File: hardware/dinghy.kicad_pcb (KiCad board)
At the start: 2 copper layers, 105.5 x 88.9 mm, 56 parts, among them J10 Header 1, J11 Header 2, J2 Fan 1, J3 Fan2, J4 Motor, J5 Endtemp, J6 Endstop, J7 PGM, J8 UART, J9 Power, Q1 IRLR7843PbF, Q2 IRLR7843PbF, Q3 IRLR7843PbF, SW1 SW_Push, U1 TMC2130, U2 ATMEGA1284P-AU, Y1 Crystal

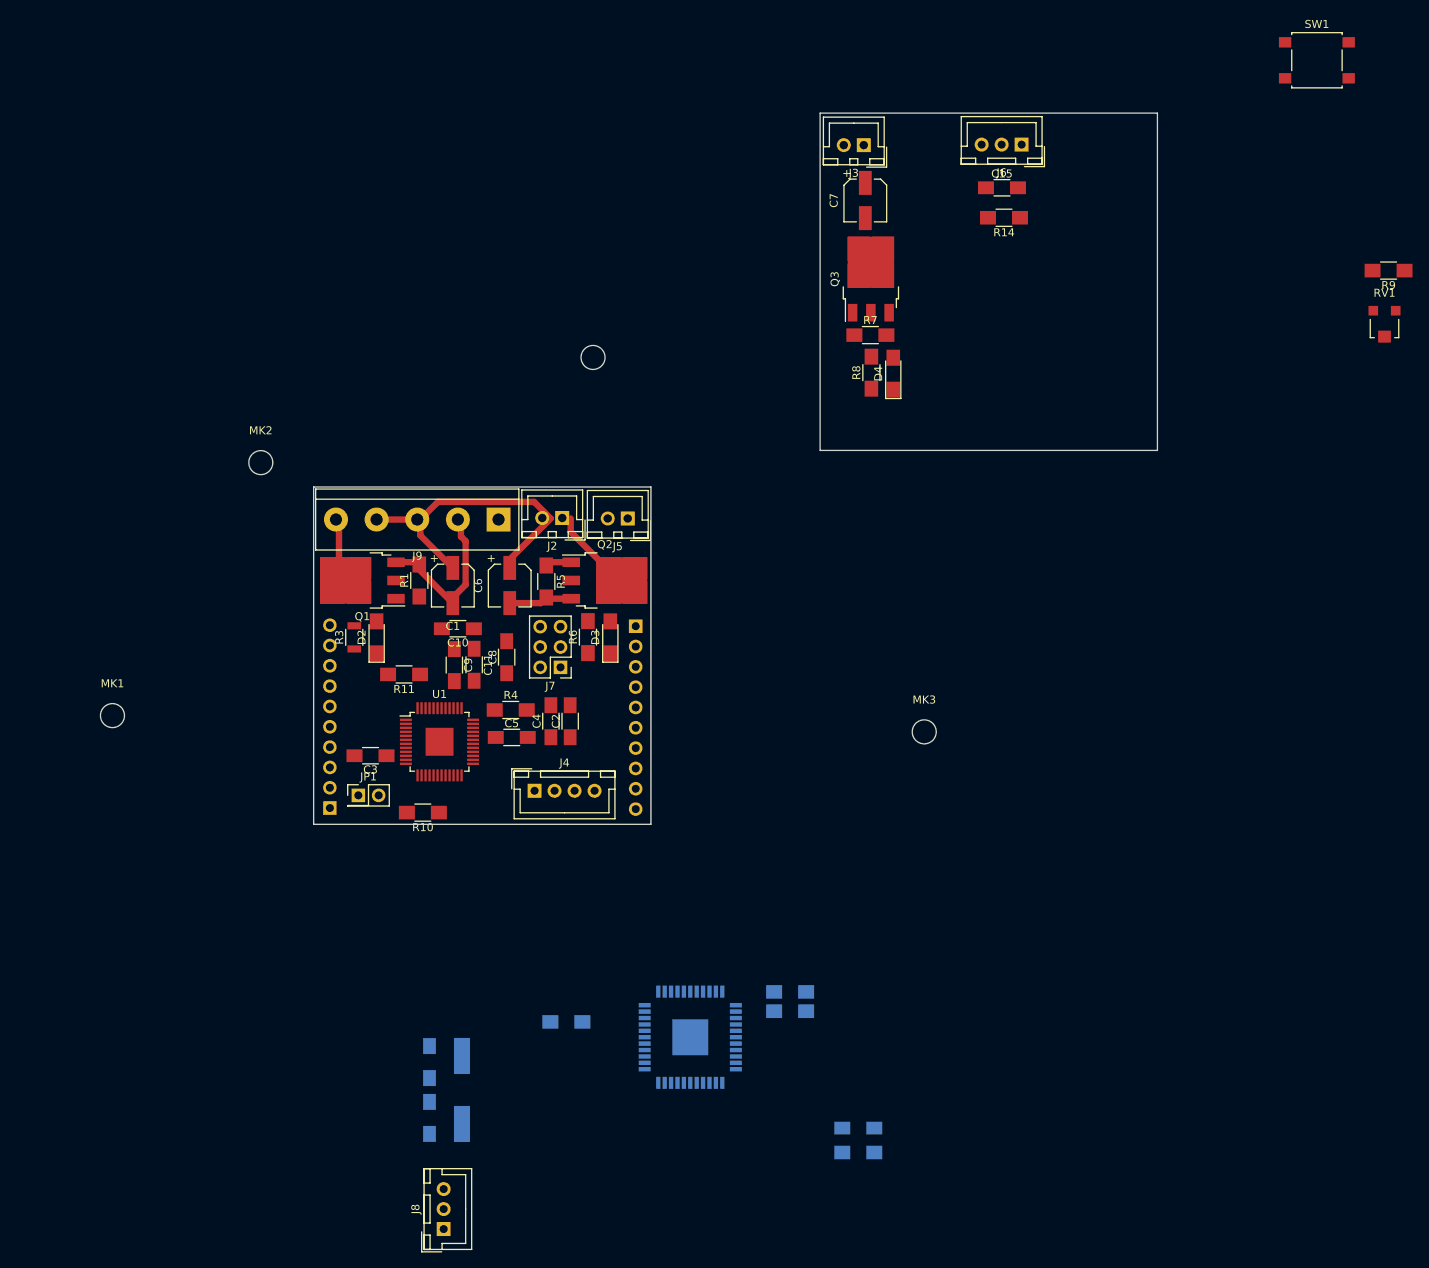
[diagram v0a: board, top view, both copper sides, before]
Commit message: Renamed power net
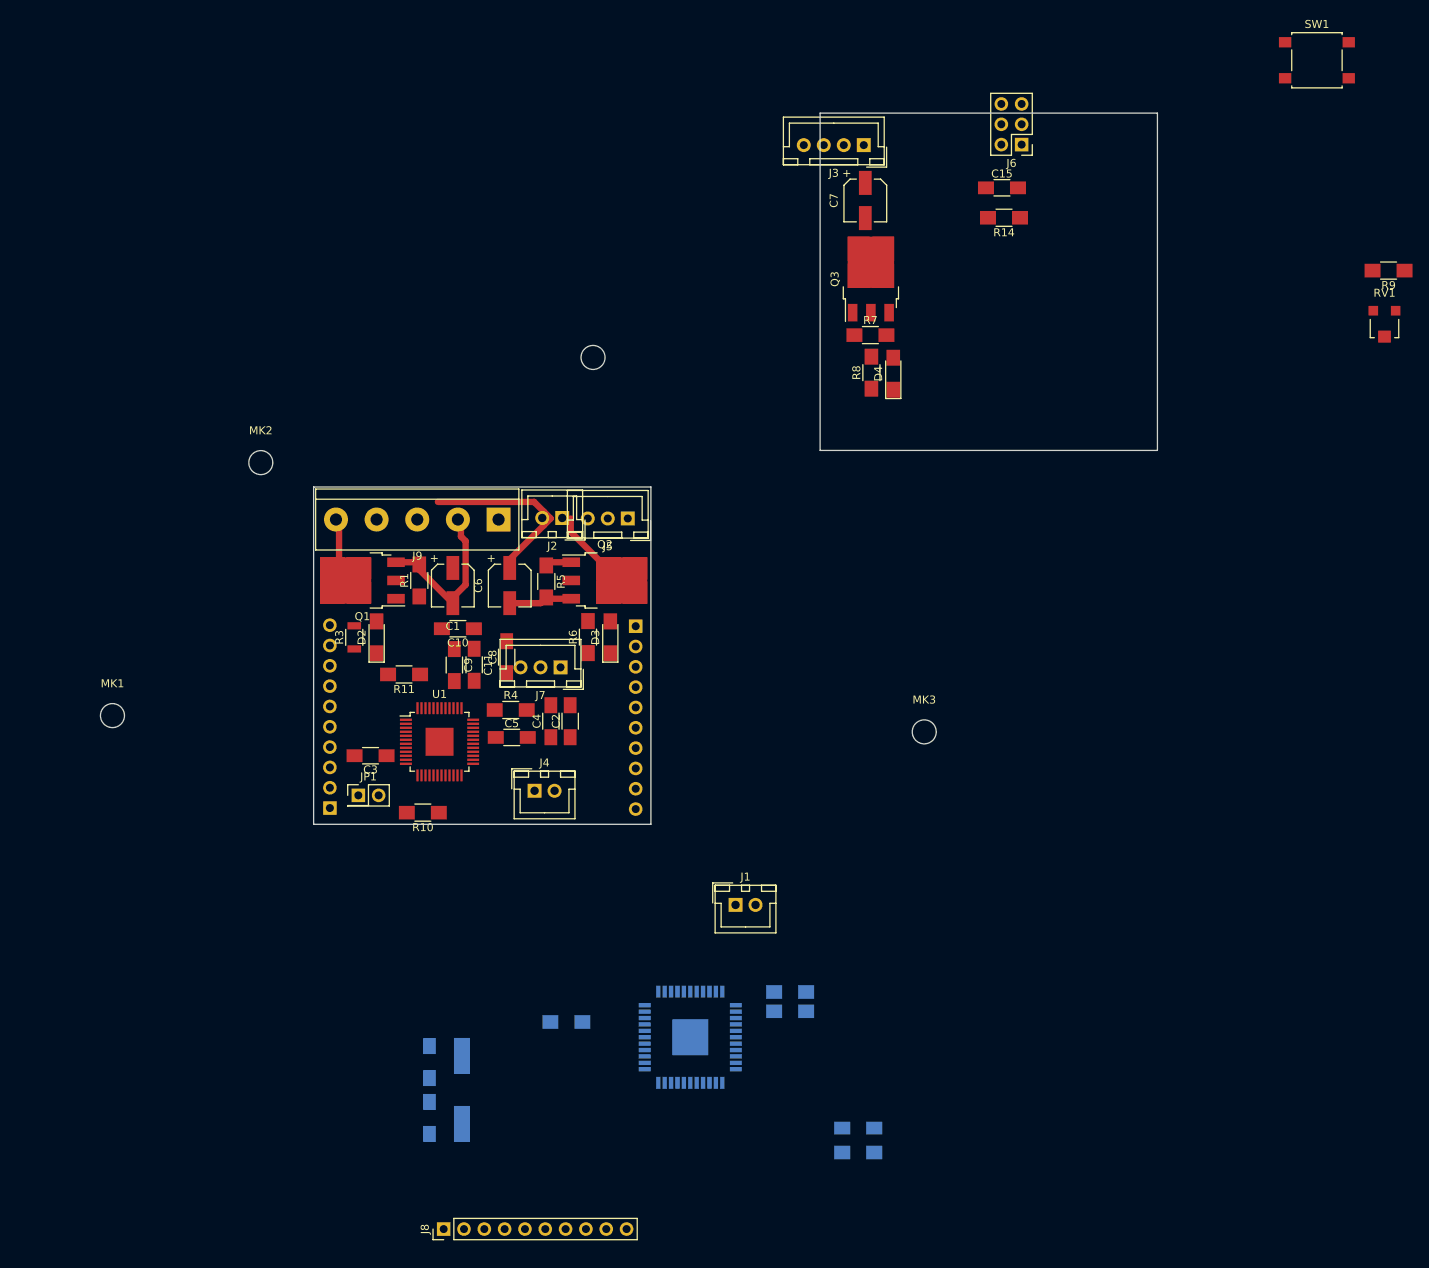
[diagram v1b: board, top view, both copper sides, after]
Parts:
- added J1: Fan 1, Connectors_JST:JST_XH_B02B-XH-A_02x2.50mm_Straight, F.Cu at (177.2, 131.5)
- C10: value 1µ/50V -> 100n/50V
- C11: value 100n/50V -> 1µ/50V
- J10: value Header 1 -> Header 2
- J2: value Fan 1 -> Fan2
- J3: value Fan2 -> Motor; footprint Connectors_JST:JST_XH_B02B-XH-A_02x2.50mm_Straight -> Connectors_JST:JST_XH_B04B-XH-A_04x2.50mm_Straight
- J4: value Motor -> Endtemp; footprint Connectors_JST:JST_XH_B04B-XH-A_04x2.50mm_Straight -> Connectors_JST:JST_XH_B02B-XH-A_02x2.50mm_Straight
- J5: value Endtemp -> Endstop; footprint Connectors_JST:JST_XH_B02B-XH-A_02x2.50mm_Straight -> Connectors_JST:JST_XH_B03B-XH-A_03x2.50mm_Straight
- J6: value Endstop -> PGM; footprint Connectors_JST:JST_XH_B03B-XH-A_03x2.50mm_Straight -> Pin_Headers:Pin_Header_Straight_2x03_Pitch2.54mm
- J7: value PGM -> UART; footprint Pin_Headers:Pin_Header_Straight_2x03_Pitch2.54mm -> Connectors_JST:JST_XH_B03B-XH-A_03x2.50mm_Straight
- J8: value UART -> Header 1; footprint Connectors_JST:JST_XH_B03B-XH-A_03x2.50mm_Straight -> Pin_Headers:Pin_Header_Straight_1x10_Pitch2.54mm
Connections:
- C1 pad 1: +12V -> VMot
- C10 pad 1: GND -> VMot
- C10 pad 2: +12V -> Net-(C10-Pad2)
- C11 pad 1: +12V -> GND
- C11 pad 2: Net-(C11-Pad2) -> VMot
- C2 pad 2: +12V -> VMot
- C6 pad 1: +12V -> VMot
- C7 pad 1: +12V -> VMot
- C9 pad 2: +12V -> VMot
- D2 pad 2: +12V -> VMot
- D3 pad 2: +12V -> VMot
- D4 pad 2: +12V -> VMot
- J10 pad 1: /PA4 -> VMot
- J10 pad 10: /SCL -> /PD4
- J10 pad 2: /PA3 -> VMot
- J10 pad 3: /PA2 -> GND
- J10 pad 4: /PA1 -> GND
- J10 pad 5: /PA0 -> +5V
- J10 pad 6: /TXD1 -> /FAN2
- J10 pad 7: /RXD1 -> /ENDSTOP
- J10 pad 8: GND -> /PD7
- J10 pad 9: /SDA -> /PD6
- J11 pad 1: /12V -> +12V
- J11 pad 2: /12V -> +12V
- J11 pad 5: (no net) -> +5V
- J2 pad 2: +12V -> VMot
- J3 pad 1: Net-(J3-Pad1) -> /OB2
- J3 pad 2: +12V -> /OB1
- J4 pad 1: /OB2 -> GND
- J4 pad 2: /OB1 -> /ENDTEMP
- J5 pad 2: /ENDTEMP -> +5V
- J6 pad 1: GND -> /MISO
- J6 pad 3: /ENDSTOP -> /SCK
- J7 pad 1: /MISO -> /TXD0
- J7 pad 2: +5V -> GND
- J7 pad 3: /SCK -> /RXD0
- J8 pad 1: /TXD0 -> /PA4
- J8 pad 2: GND -> /PA3
- J8 pad 3: /RXD0 -> /PA2
- J9 pad 3: +12V -> VMot
- J9 pad 4: +12V -> VMot
- Q2 pad 2: Net-(J2-Pad1) -> Net-(J1-Pad1)
- Q3 pad 2: Net-(J3-Pad1) -> Net-(J2-Pad1)
- R6 pad 2: Net-(J2-Pad1) -> Net-(J1-Pad1)
- R8 pad 2: Net-(J3-Pad1) -> Net-(J2-Pad1)
- U1 pad 21: +12V -> VMot
- U1 pad 24: (no net) -> /M-DCEN
- U1 pad 27: (no net) -> /M-DIAG1
- U1 pad 38: Net-(C11-Pad2) -> Net-(C10-Pad2)
- U1 pad 39: +12V -> VMot
- U1 pad 40: +12V -> VMot
- U2 pad 22: (no net) -> /M-DCEN
- U2 pad 26: (no net) -> /M-DIAG1
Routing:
- net +12V: track 39.2 -> 0.00 mm
- net VMot: track 0.00 -> 23.3 mm
- net Net-(J2-Pad1): track 8.26 -> 0.00 mm
- net Net-(J1-Pad1): track 0.00 -> 8.26 mm

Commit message: Basic layout done.
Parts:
- removed J11: Header 2, Pin_Headers:Pin_Header_Straight_1x10_Pitch2.54mm
- D1, MK4, R2: moved to F.Cu
- J8: moved to B.Cu
- R3: footprint Resistors_SMD:R_1206 -> Resistors_SMD:R_1206_HandSoldering
- moved J6 111.2 mm to (135.5, 116.2), turned to 270 degrees
- moved J3 96.1 mm to (141.5, 117.5), turned to 0 degrees
- moved C12 65.9 mm to (147.0, 92.7), turned to 180 degrees
- moved C13 60.4 mm to (154.0, 92.7), turned to 0 degrees
- moved J5 60.2 mm to (216.1, 53.6)
- moved Y1 58.4 mm to (150.5, 96.7), turned to 180 degrees
- moved J8 54.8 mm to (126.4, 119.1), turned to 0 degrees
- moved J1 54.3 mm to (153.0, 82.9)
- moved D1 46.9 mm to (158.7, 105.3), turned to 270 degrees
- moved U2 44.7 mm to (155.0, 106.5), turned to 270 degrees
- moved R2 43.4 mm to (161.5, 105.3), turned to 270 degrees
- moved JP1 41.5 mm to (88.6, 115.3), turned to 270 degrees
- moved R12 41.1 mm to (175.4, 109.8), turned to 180 degrees
- moved J2 37.6 mm to (183.2, 57.7)
- moved J4 35.5 mm to (161.2, 82.9)
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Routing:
- net GND: track 29.0 -> 0.00 mm
- net VMot: track 23.3 -> 0.00 mm
- net Net-(J1-Pad1): track 8.26 -> 0.00 mm
- net /HOTEND-: track 6.45 -> 0.00 mm
- net /FAN1: track 3.29 -> 0.00 mm
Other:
- net class Digital added: clearance 0.2, trace_width 0.2, via_dia 0.6, via_drill 0.4
- net class Power added: clearance 0.3, trace_width 0.8, via_dia 0.6, via_drill 0.4

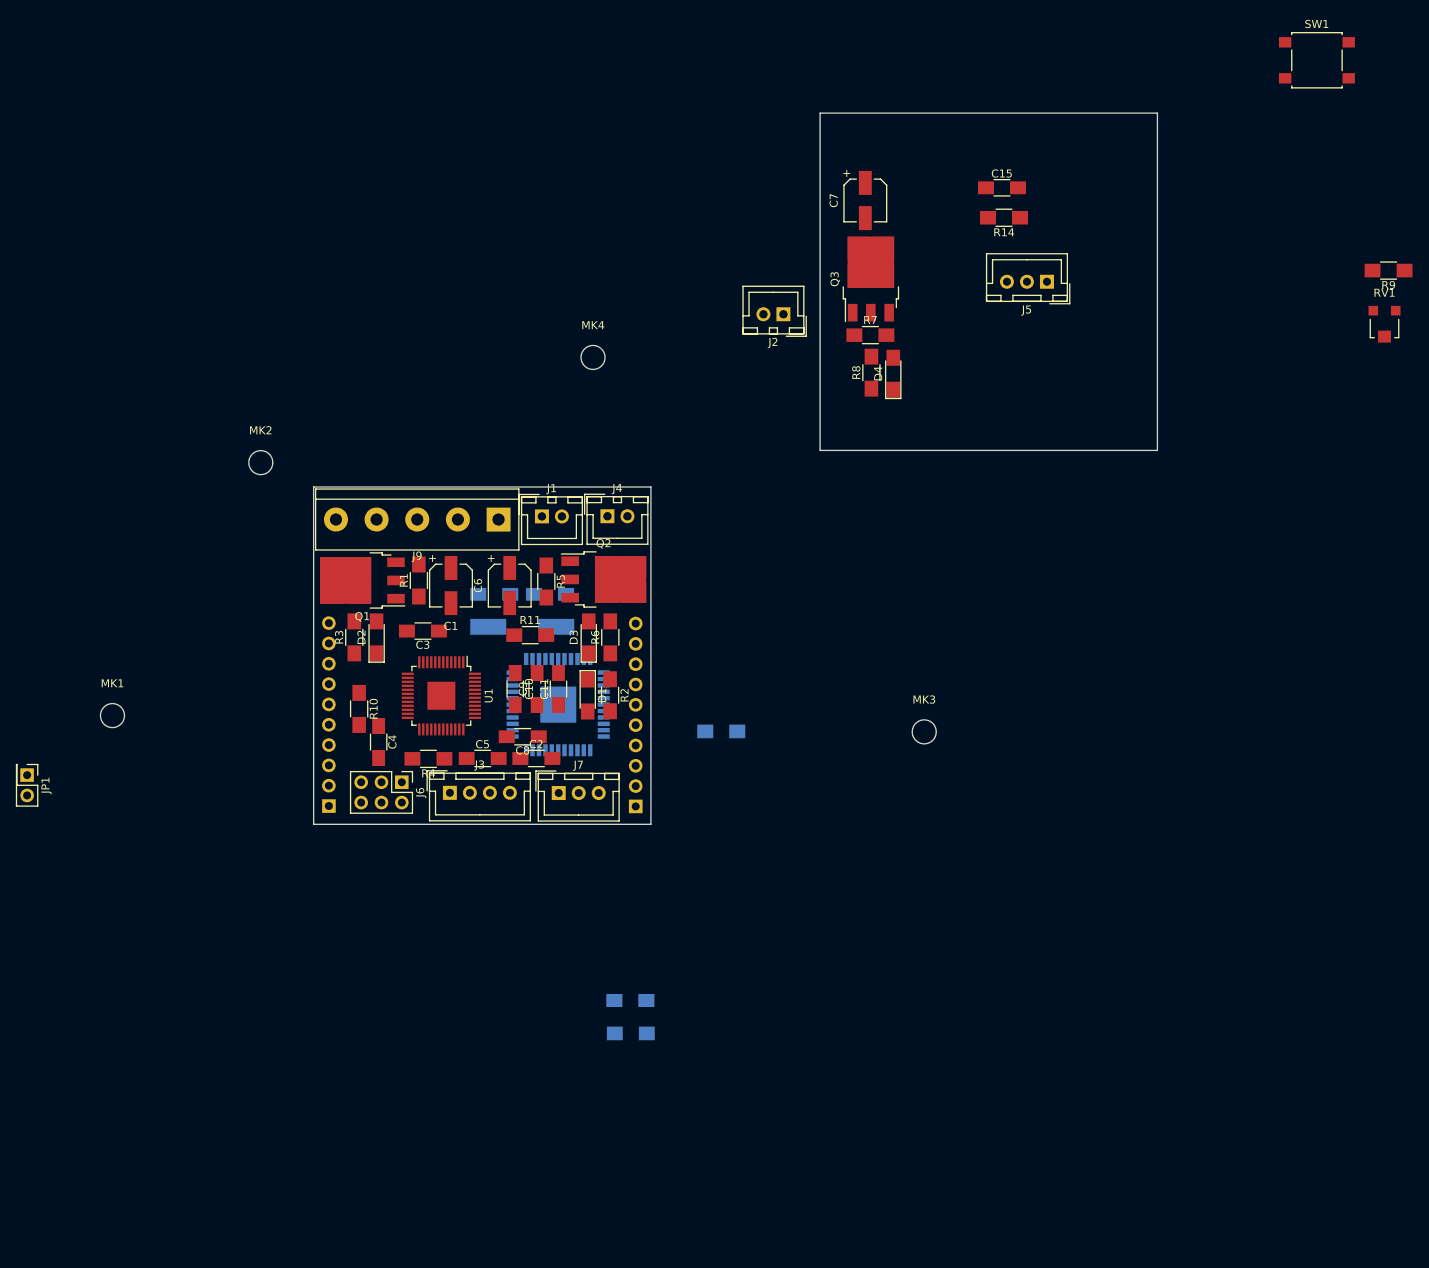
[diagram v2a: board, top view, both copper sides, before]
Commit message: Split second board of to seperate schematic
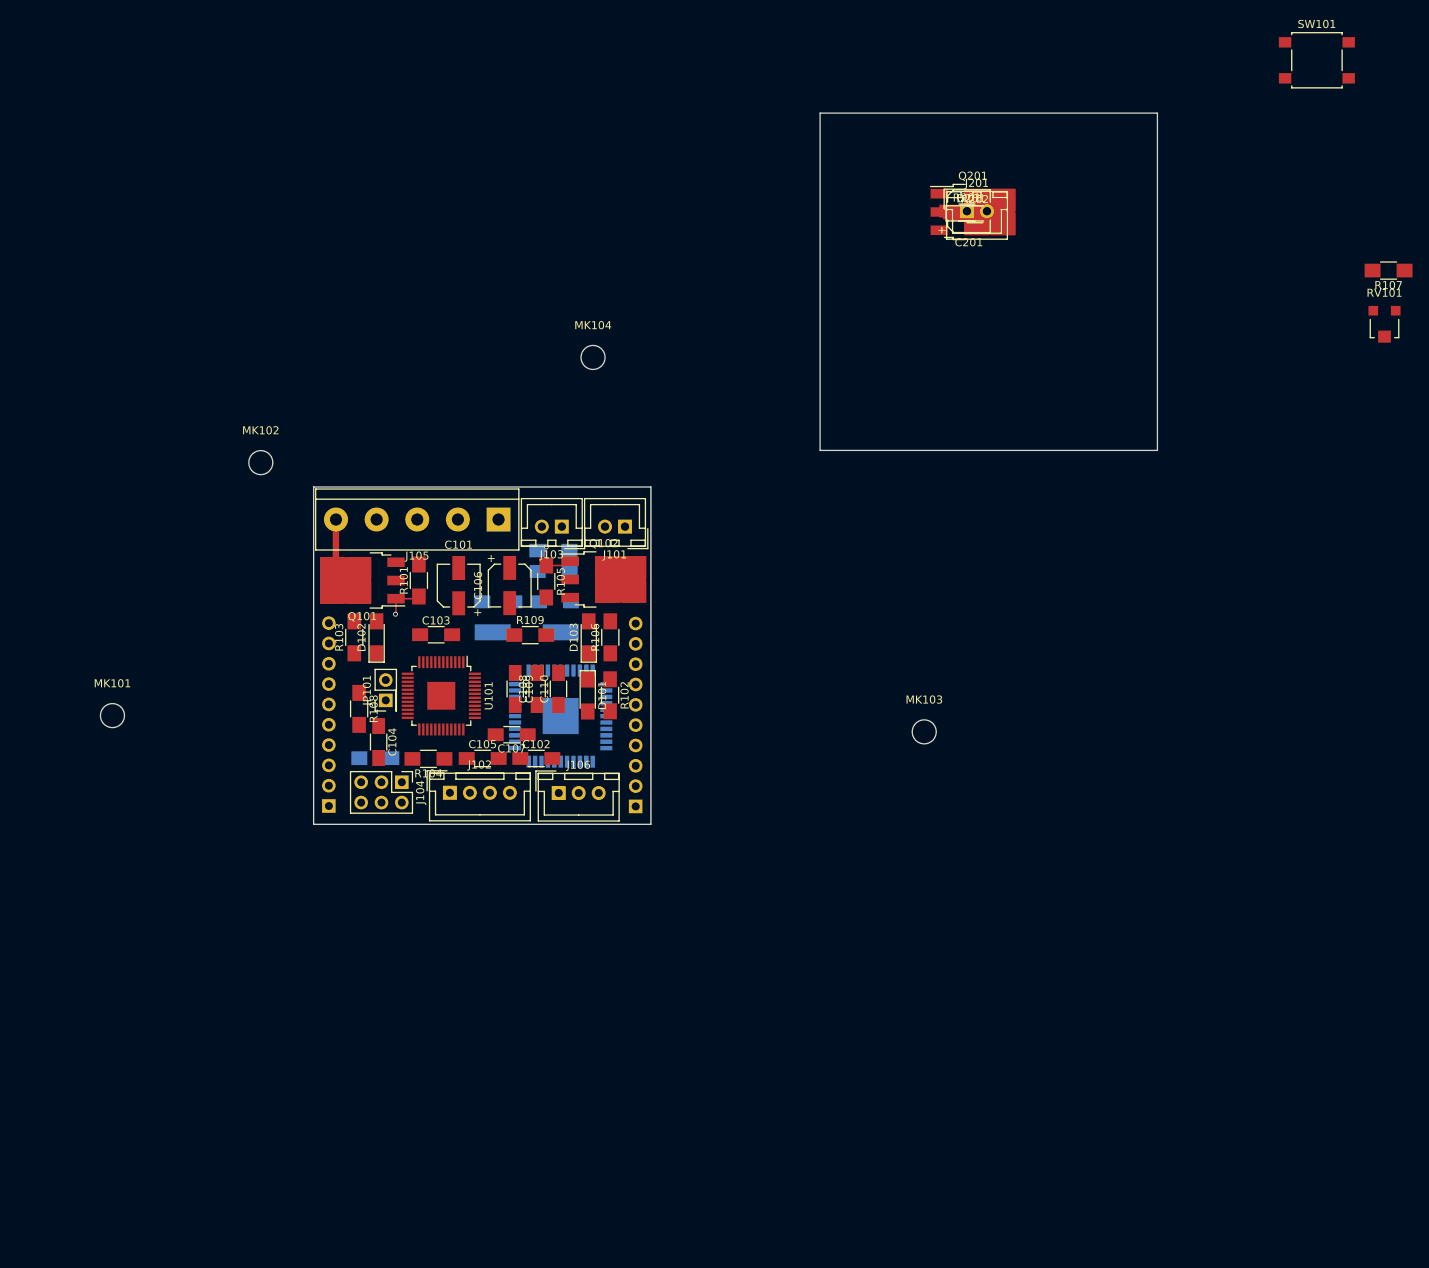
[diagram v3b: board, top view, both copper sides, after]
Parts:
- removed C15: 10µ, Capacitors_SMD:C_1206_HandSoldering
- removed C7: 100µ/35V, Capacitors_SMD:CP_Elec_5x5.8
- removed D4: LED, LEDs:LED_1206_HandSoldering
- removed J2: Fan2, Connectors_JST:JST_XH_B02B-XH-A_02x2.50mm_Straight
- removed J5: Endstop, Connectors_JST:JST_XH_B03B-XH-A_03x2.50mm_Straight
- removed Q3: IRLR7843PbF, TO_SOT_Packages_SMD:TO-252-3_TabPin2
- removed R14, R7: 10k, Resistors_SMD:R_1206_HandSoldering
- removed R8: 4k7, Resistors_SMD:R_1206_HandSoldering
- added C201: 100µ/35V, Capacitors_SMD:CP_Elec_5x5.8, F.Cu at (206.4, 44.8)
- added D201: LED, LEDs:LED_1206_HandSoldering, F.Cu at (206.6, 45.0)
- added J201: Fan2, Connectors_JST:JST_XH_B02B-XH-A_02x2.50mm_Straight, F.Cu at (206.1, 44.8)
- added Q201: IRLR7843PbF, TO_SOT_Packages_SMD:TO-252-3_TabPin2, F.Cu at (206.9, 44.9)
- added R201: 10k, Resistors_SMD:R_1206_HandSoldering, F.Cu at (206.1, 44.9)
- added R202: 4k7, Resistors_SMD:R_1206_HandSoldering, F.Cu at (207.1, 45.1)
- moved R111 61.1 mm to (154.4, 87.2), turned to 0 degrees
- moved C113 54.5 mm to (154.5, 89.8), turned to 180 degrees
- moved JP101 45.8 mm to (133.5, 105.9), turned to 90 degrees
- moved R110 43.4 mm to (132.2, 113.2)
- moved J101 10.5 mm to (163.4, 84.2), turned to 180 degrees
- moved C111 7.65 mm to (154.6, 93.6)
- moved C112 6.54 mm to (147.5, 93.6)
- moved J103 5.85 mm to (155.5, 84.2), turned to 180 degrees
- moved C103 1.71 mm to (139.8, 97.7), turned to 0 degrees
- moved U102 1.47 mm to (155.3, 107.9)
- moved C107 1.39 mm to (149.2, 110.2)
- moved C101 0.97 mm to (142.6, 91.6), turned to 90 degrees
- moved Y101 0.89 mm to (151.1, 97.4)
- renumbered C1 to C101, C2 to C102, C3 to C103, C4 to C104, C5 to C105, C6 to C106, C8 to C107, C9 to C108, C10 to C109, C11 to C110, C12 to C111, C13 to C112, C14 to C113, D1 to D101, D2 to D102, D3 to D103, J1 to J101, J3 to J102, J4 to J103, J6 to J104, J9 to J105, J7 to J106, J8 to J107, J10 to J108, JP1 to JP101, MK1 to MK101, MK2 to MK102, MK3 to MK103, MK4 to MK104, Q1 to Q101, Q2 to Q102, R1 to R101, R2 to R102, R3 to R103, R4 to R104, R5 to R105, R6 to R106, R9 to R107, R10 to R108, R11 to R109, R12 to R110, R13 to R111, RV1 to RV101, SW1 to SW101, U1 to U101, U2 to U102, Y1 to Y101
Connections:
- net /FAN2 renamed PB4
- net /PA0 renamed PA0
- net /PA1 renamed PA1
- net /PA2 renamed PA2
- net /PA3 renamed PA3
- net /PA4 renamed PA4
- net /PD4 renamed PD4
- net /PD6 renamed PD6
- net /PD7 renamed PD7
- net /RXD1 renamed RXD1
- net /SCL renamed SCL
- net /SDA renamed SDA
- net /TXD1 renamed TXD1
- J103 pad 1: GND -> /ENDTEMP
- J103 pad 2: /ENDTEMP -> GND
- J105 pad 2: GND -> VMot
- J105 pad 3: VMot -> GND
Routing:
- net /HOTEND-: track 0.00 -> 6.29 mm
- net /FAN1: track 0.00 -> 5.52 mm, vias 0 -> 1
- net /HOTEND: track 0.00 -> 4.94 mm, vias 0 -> 1
